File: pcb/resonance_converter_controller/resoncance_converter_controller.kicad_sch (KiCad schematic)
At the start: 53 parts, among them J2 USB_C_Receptacle_USB2.0_14P, J3 FX18-120P-0.8SV, J7 Conn_ARM_SWD_TagConnect_TC2030

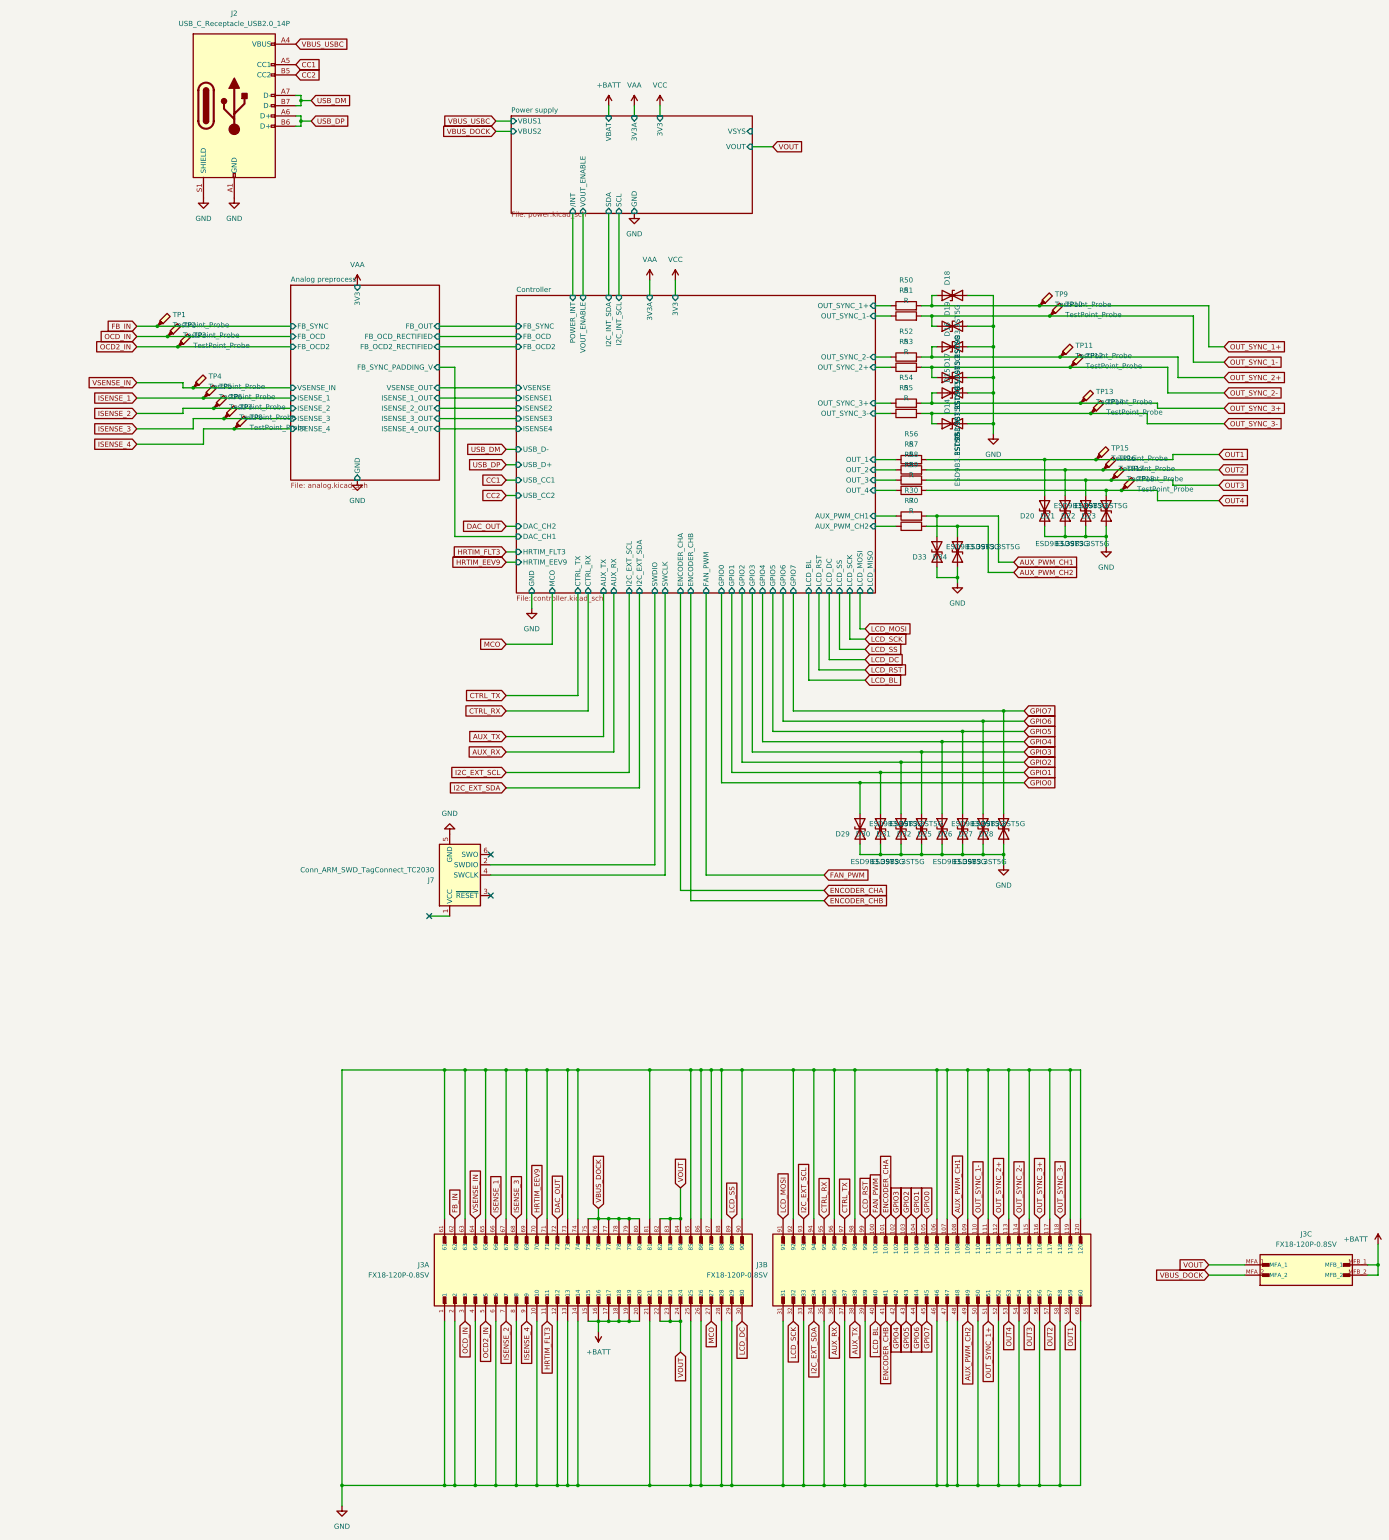
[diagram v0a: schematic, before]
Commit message: Update conector in som
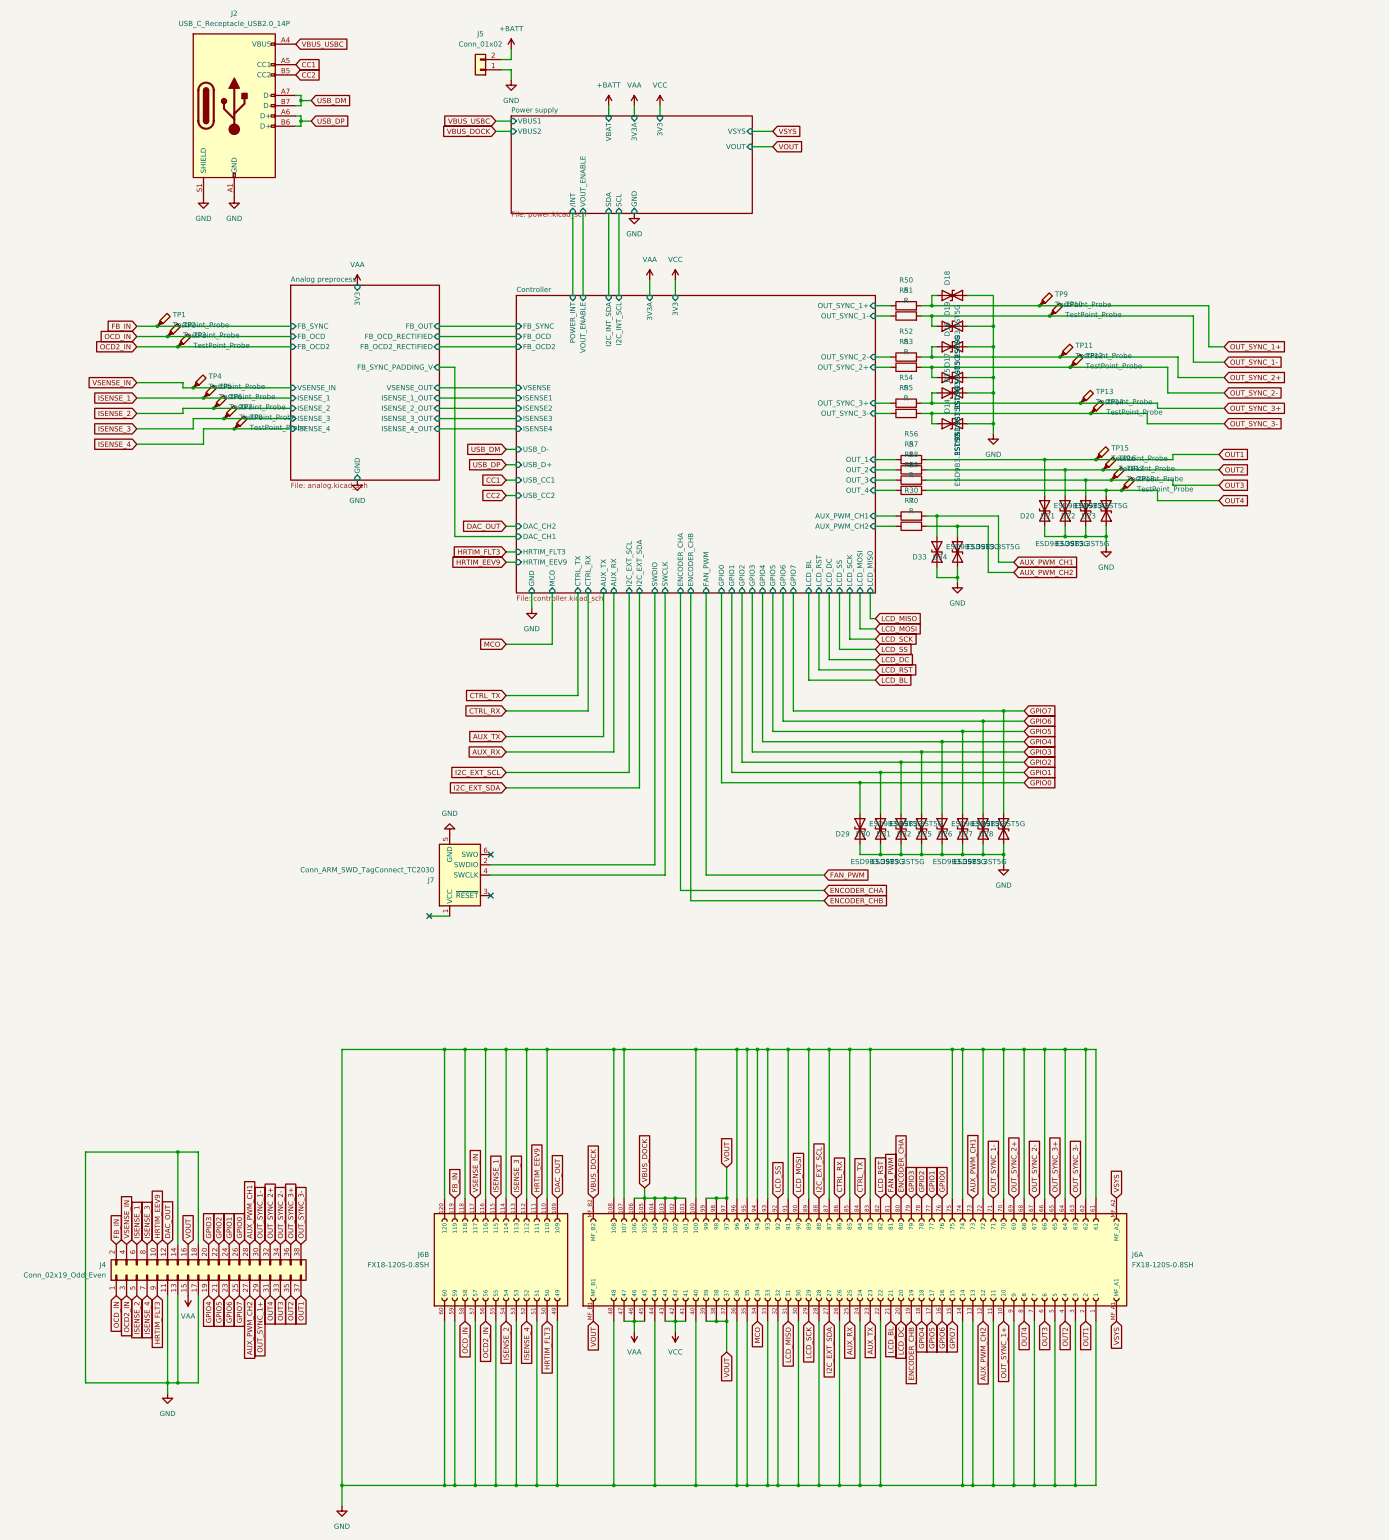
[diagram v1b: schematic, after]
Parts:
- removed J3: FX18-120P-0.8SV, FX18-120P-0.8SV:HIROSE_FX18-120P-0.8SV, symbol FX18-120P-0.8SV:FX18-120P-0.8SV
- added J4: Conn_02x19_Odd_Even, Connector_PinSocket_2.54mm:PinSocket_2x19_P2.54mm_Vertical_SMD, symbol Connector_Generic:Conn_02x19_Odd_Even
- added J5: Conn_01x02, Connector_AMASS:AMASS_XT30U-M_1x02_P5.0mm_Vertical, symbol Connector_Generic:Conn_01x02
- added J6: FX18-120S-0.8SH, FX18-120S-0.8SH:HIROSE_FX18-120S-0.8SH, symbol FX18-120S-0.8SH:FX18-120S-0.8SH
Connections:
- net +BATT: now also J5.2 (Pin_2)
- net AUX_PWM_CH1: now also J4.28 (Pin_28), J6.73
- net AUX_PWM_CH2: now also J4.27 (Pin_27), J6.12
- net AUX_RX: now also J6.25
- net AUX_TX: now also J6.23
- net CTRL_RX: now also J6.86
- net CTRL_TX: now also J6.84
- net DAC_OUT: now also J4.12 (Pin_12), J6.109
- net ENCODER_CHA: now also J6.80
- net ENCODER_CHB: now also J6.19
- net FAN_PWM: now also J6.81
- net FB_IN: now also J4.2 (Pin_2), J6.119
- net GND: now also J4.11 (Pin_11), J4.13 (Pin_13), J4.14 (Pin_14), J4.17 (Pin_17), J4.18 (Pin_18), J5.1 (Pin_1), J6.1, J6.100, J6.107, J6.108, J6.11, J6.110, J6.112, J6.114, J6.116, J6.118, J6.120, J6.13, J6.14, J6.22, J6.24, J6.26, J6.28, J6.3, J6.30, J6.32, J6.33, J6.35, J6.36, J6.40, J6.44, J6.48, J6.49, J6.5, J6.51, J6.53, J6.55, J6.57, J6.59, J6.60, J6.61, J6.62, J6.64, J6.66, J6.68, J6.7, J6.70, J6.72, J6.74, J6.75, J6.83, J6.85, J6.87, J6.89, J6.9, J6.91, J6.93, J6.94, J6.95, J6.96
- net GPIO0: now also J4.26 (Pin_26), J6.76
- net GPIO1: now also J4.24 (Pin_24), J6.77
- net GPIO2: now also J4.22 (Pin_22), J6.78
- net GPIO3: now also J4.20 (Pin_20), J6.79
- net GPIO4: now also J4.19 (Pin_19), J6.18
- net GPIO5: now also J4.21 (Pin_21), J6.17
- net GPIO6: now also J4.23 (Pin_23), J6.16
- net GPIO7: now also J4.25 (Pin_25), J6.15
- net HRTIM_EEV9: now also J4.10 (Pin_10), J6.111
- net HRTIM_FLT3: now also J4.9 (Pin_9), J6.50
- net I2C_EXT_SCL: now also J6.88
- net I2C_EXT_SDA: now also J6.27
- net ISENSE_1: now also J4.6 (Pin_6), J6.115
- net ISENSE_2: now also J4.5 (Pin_5), J6.54
- net ISENSE_3: now also J4.8 (Pin_8), J6.113
- net ISENSE_4: now also J4.7 (Pin_7), J6.52
- net LCD_BL: now also J6.21
- net LCD_DC: now also J6.20
- net LCD_MOSI: now also J6.90
- net LCD_RST: now also J6.82
- net LCD_SCK: now also J6.29
- net LCD_SS: now also J6.92
- net MCO: now also J6.34
- net OCD2_IN: now also J4.3 (Pin_3), J6.56
- net OCD_IN: now also J4.1 (Pin_1), J6.58
- net OUT1: now also J4.37 (Pin_37), J6.2
- net OUT2: now also J4.35 (Pin_35), J6.4
- net OUT3: now also J4.33 (Pin_33), J6.6
- net OUT4: now also J4.31 (Pin_31), J6.8
- net OUT_SYNC_1+: now also J4.29 (Pin_29), J6.10
- net OUT_SYNC_1-: now also J4.30 (Pin_30), J6.71
- net OUT_SYNC_2+: now also J4.32 (Pin_32), J6.69
- net OUT_SYNC_2-: now also J4.34 (Pin_34), J6.67
- net OUT_SYNC_3+: now also J4.36 (Pin_36), J6.65
- net OUT_SYNC_3-: now also J4.38 (Pin_38), J6.63
- net VAA: now also J4.15 (Pin_15), J6.45, J6.46, J6.47
- net VBUS_DOCK: now also J6.101, J6.102, J6.103, J6.104, J6.105, J6.106, J6.MF_B2
- net VCC: now also J6.41, J6.42, J6.43
- net VOUT: now also J4.16 (Pin_16), J6.37, J6.38, J6.39, J6.97, J6.98, J6.99, J6.MF_B1
- net VSENSE_IN: now also J4.4 (Pin_4), J6.117
- new net LCD_MISO: J6.31
- new net VSYS: J6.MF_A1, J6.MF_A2

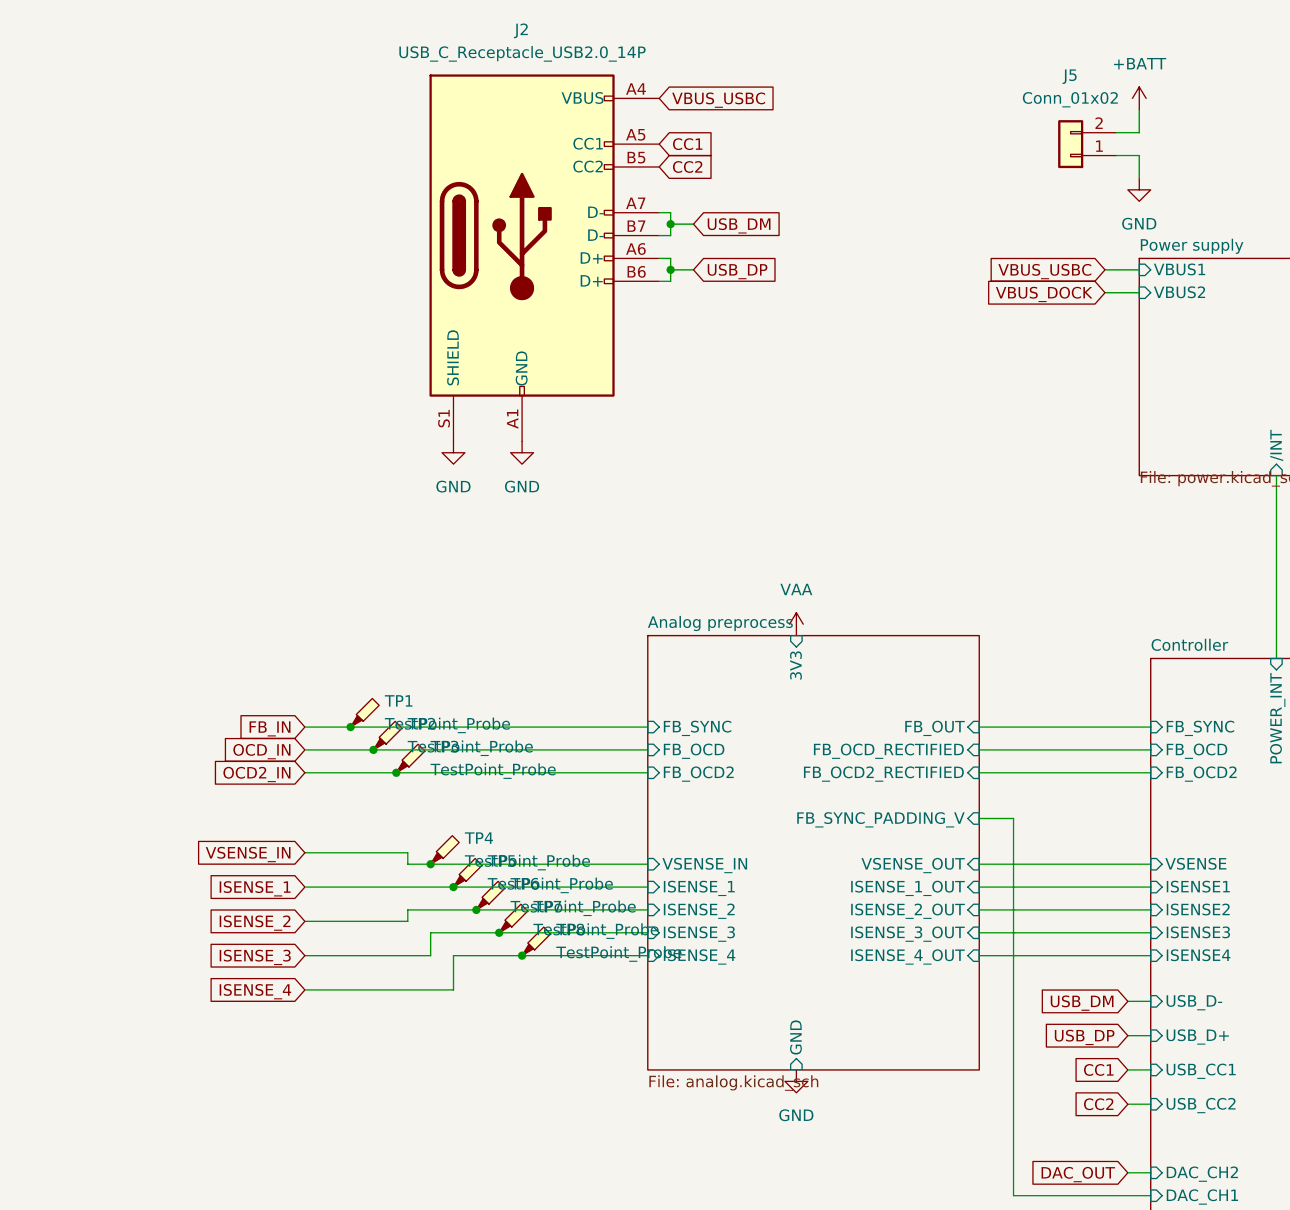
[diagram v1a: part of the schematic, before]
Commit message: First routing without testpoints
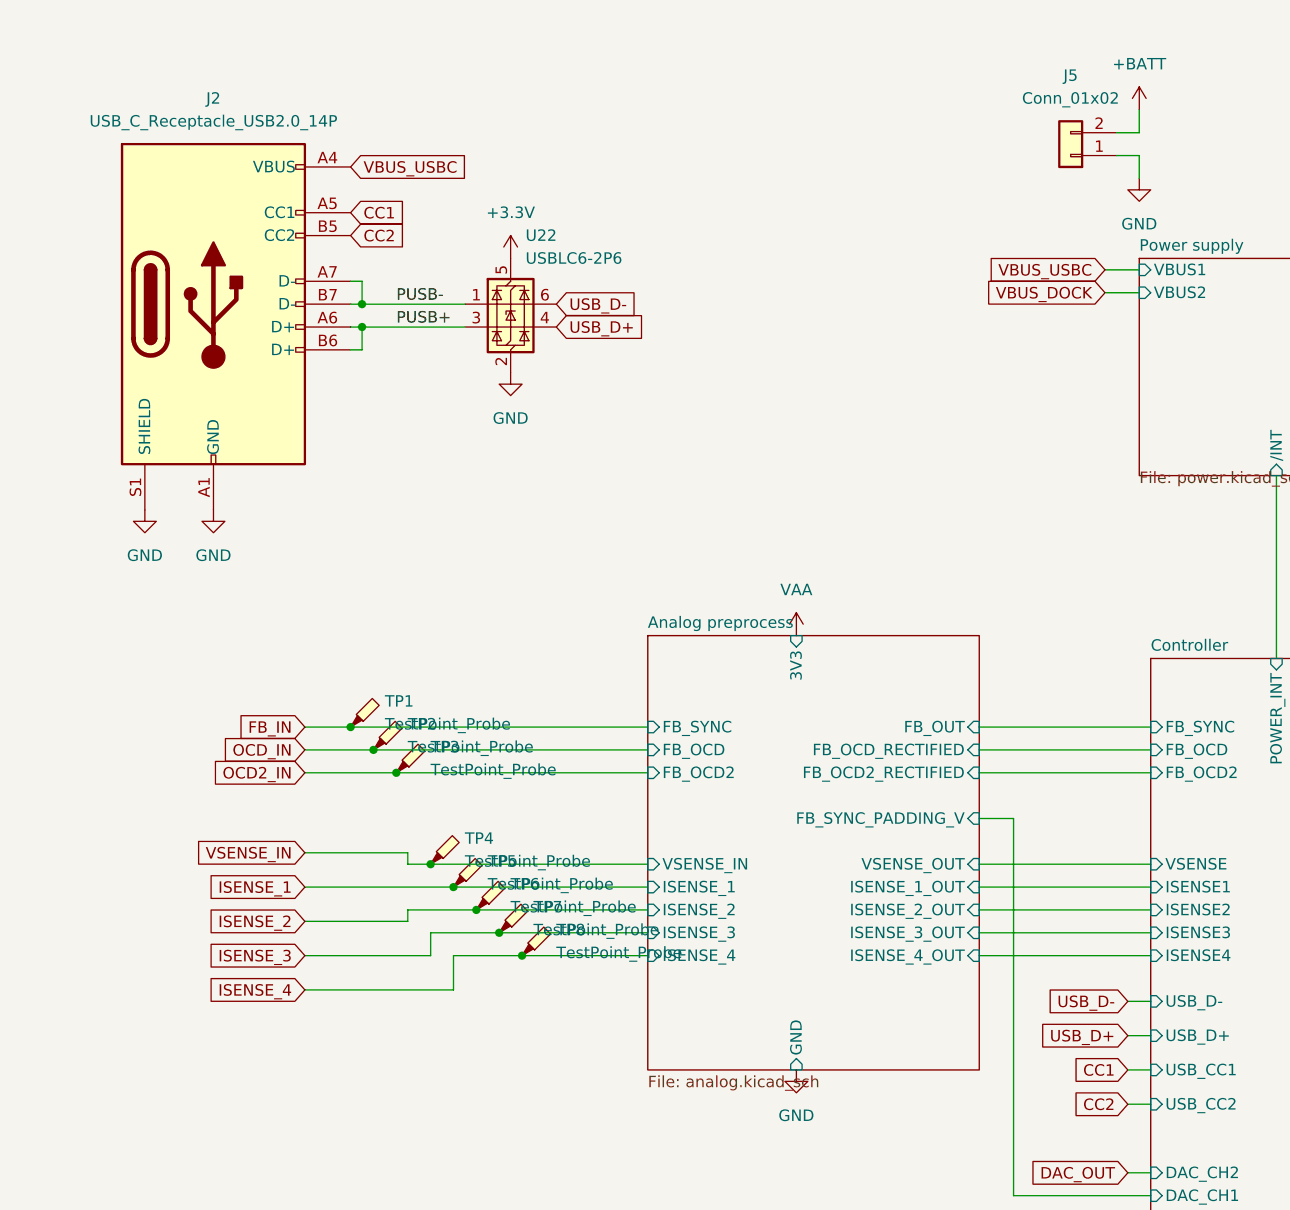
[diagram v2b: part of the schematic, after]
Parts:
- added U22: USBLC6-2P6, Package_TO_SOT_SMD:SOT-666, symbol Power_Protection:USBLC6-2P6
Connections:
- net GND: now also U22.2 (GND)
- net USB_DM renamed PUSB-
- net PUSB-: now also U22.1 (I/O1)
- net USB_DP renamed PUSB+
- net PUSB+: now also U22.3 (I/O2)
- new net +3.3V: U22.5 (VBUS)
- new net USB_D+: U22.4 (I/O2)
- new net USB_D-: U22.6 (I/O1)
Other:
- moved on the sheet: J2
